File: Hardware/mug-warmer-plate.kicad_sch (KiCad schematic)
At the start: 32 parts, among them SW1 SW_DIP_x01, U1 LM35-NEB, U2 ATtiny85-20P

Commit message: Added test point to test thermoelectric cooler
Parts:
- added TP3, TP4: (no value), symbol Connector:TestPoint
- C9: value (none) -> 1uF; footprint (none) -> Capacitor_THT:C_Disc_D4.3mm_W1.9mm_P5.00mm
- J1: value (none) -> USB_C_Receptacle_USB2.0; footprint (none) -> USB_C_Power:TYPE-C-31-M-17
- J4: value (none) -> Conn_01x02_Male; footprint (none) -> Connector_PinHeader_2.54mm:PinHeader_1x04_P2.54mm_Vertical
- NT1: value (none) -> NetTie_2
- Q1: value (none) -> IRLZ44N; footprint (none) -> Package_TO_SOT_THT:TO-220-3_Vertical
- R1, R2, R3, R4, R5, R6, R7, R8: footprint (none) -> Resistor_THT:R_Axial_DIN0207_L6.3mm_D2.5mm_P10.16mm_Horizontal
- SW1: footprint (none) -> Button_Switch_THT:SW_PUSH_6mm_H4.3mm
- TP1, TP2: footprint (none) -> TestPoint:TestPoint_Pad_2.0x2.0mm
- U1: footprint (none) -> Package_TO_SOT_THT:TO-220-3_Horizontal_TabDown
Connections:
- net +5V: now also TP3.1
- net at C5.1, D2.1 (K), NT2.1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: now also TP4.1
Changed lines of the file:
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@@
     (company "KMBS Labs")
   )
+  (junction (at 139.7 162.56) (diameter 0) (color 0 0 0 0)
+  )
   (junction (at 121.92 140.97) (diameter 0) (color 0 0 0 0)
+  )
+  (junction (at 138.43 140.97) (diameter 0) (color 0 0 0 0)
   )
   (junction (at 242.57 101.6) (diameter 0) (color 0 0 0 0)
@@
     (in_bom yes) (on_board yes) (fields_autoplaced)
     (property "Reference" "NT1" (id 0) (at 140.97 135.89 0))
-    (property "Value" "" (id 1) (at 140.97 138.43 0))
+    (property "Value" "NetTie_2" (id 1) (at 140.97 138.43 0))
     (property "Footprint" "NetTie:NetTie-2_SMD_Pad0.5mm" (id 2) (at 140.97 140.97 0)
       (effects (font (size 1.27 1.27)) hide)
@@
     (pin "1")
   )
+  (symbol (lib_id "Connector:TestPoint") (at 139.7 162.56 0) (unit 1)
+    (in_bom yes) (on_board yes) (fields_autoplaced)
+    (property "Reference" "TP4" (id 0) (at 142.24 157.9879 0)
+      (effects (font (size 1.27 1.27)) (justify left))
+    )
+    (property "Value" "" (id 1) (at 142.24 160.5279 0)
+      (effects (font (size 1.27 1.27)) (justify left))
+    )
+    (property "Footprint" "" (id 2) (at 144.78 162.56 0)
+      (effects (font (size 1.27 1.27)) hide)
+    )
+    (property "Datasheet" "~" (id 3) (at 144.78 162.56 0)
+      (effects (font (size 1.27 1.27)) hide)
+    )
+    (pin "1")
+  )
   (symbol (lib_id "Device:R") (at 234.95 116.84 0) (unit 1)
     (in_bom yes) (on_board yes) (fields_autoplaced)
@@
       (effects (font (size 1.27 1.27)) (justify left))
     )
-    (property "Footprint" "" (id 2) (at 233.172 116.84 90)
+    (property "Footprint" "Resistor_THT:R_Axial_DIN0207_L6.3mm_D2.5mm_P10.16mm_Horizontal" (id 2) (at 233.172 116.84 90)
       (effects (font (size 1.27 1.27)) hide)
     )
@@
       (effects (font (size 1.27 1.27)) (justify right))
     )
-    (property "Value" "" (id 1) (at 255.27 104.1399 0)
-      (effects (font (size 1.27 1.27)) (justify right))
-    )
-    (property "Footprint" "" (id 2) (at 254 104.14 0)
+    (property "Value" "Conn_01x02_Male" (id 1) (at 255.27 104.1399 0)
+      (effects (font (size 1.27 1.27)) (justify right))
+    )
+    (property "Footprint" "Connector_PinHeader_2.54mm:PinHeader_1x04_P2.54mm_Vertical" (id 2) (at 254 104.14 0)
       (effects (font (size 1.27 1.27)) hide)
     )
@@
       (effects (font (size 1.27 1.27)) (justify left))
     )
-    (property "Footprint" "" (id 2) (at 121.412 179.07 90)
+    (property "Footprint" "Resistor_THT:R_Axial_DIN0207_L6.3mm_D2.5mm_P10.16mm_Horizontal" (id 2) (at 121.412 179.07 90)
       (effects (font (size 1.27 1.27)) hide)
     )
@@
       (effects (font (size 1.27 1.27)) (justify left))
     )
-    (property "Footprint" "" (id 2) (at 224.282 116.84 90)
+    (property "Footprint" "Resistor_THT:R_Axial_DIN0207_L6.3mm_D2.5mm_P10.16mm_Horizontal" (id 2) (at 224.282 116.84 90)
       (effects (font (size 1.27 1.27)) hide)
     )
@@
     (in_bom yes) (on_board yes) (fields_autoplaced)
     (property "Reference" "J1" (id 0) (at 38.1 27.94 0))
-    (property "Value" "" (id 1) (at 38.1 30.48 0))
-    (property "Footprint" "" (id 2) (at 41.91 50.8 0)
+    (property "Value" "USB_C_Receptacle_USB2.0" (id 1) (at 38.1 30.48 0))
+    (property "Footprint" "USB_C_Power:TYPE-C-31-M-17" (id 2) (at 41.91 50.8 0)
       (effects (font (size 1.27 1.27)) hide)
     )
@@
       (effects (font (size 1.27 1.27)) (justify right))
     )
-    (property "Value" "" (id 1) (at 111.76 180.34 0)
-      (effects (font (size 1.27 1.27)) (justify right))
-    )
-    (property "Footprint" "" (id 2) (at 117.1448 175.26 0)
+    (property "Value" "1uF" (id 1) (at 111.76 180.34 0)
+      (effects (font (size 1.27 1.27)) (justify right))
+    )
+    (property "Footprint" "Capacitor_THT:C_Disc_D4.3mm_W1.9mm_P5.00mm" (id 2) (at 117.1448 175.26 0)
       (effects (font (size 1.27 1.27)) hide)
     )
@@
       (effects (font (size 1.27 1.27)) (justify left))
     )
-    (property "Footprint" "" (id 2) (at 97.79 45.72 0)
+    (property "Footprint" "TestPoint:TestPoint_Pad_2.0x2.0mm" (id 2) (at 97.79 45.72 0)
       (effects (font (size 1.27 1.27)) hide)
     )
@@
       (effects (font (size 1.27 1.27)) (justify left))
     )
-    (property "Footprint" "" (id 2) (at 240.792 116.84 90)
+    (property "Footprint" "Resistor_THT:R_Axial_DIN0207_L6.3mm_D2.5mm_P10.16mm_Horizontal" (id 2) (at 240.792 116.84 90)
       (effects (font (size 1.27 1.27)) hide)
     )
@@
       (effects (font (size 1.27 1.27)) (justify right))
     )
-    (property "Footprint" "" (id 2) (at 266.7 71.12 0)
+    (property "Footprint" "Button_Switch_THT:SW_PUSH_6mm_H4.3mm" (id 2) (at 266.7 71.12 0)
       (effects (font (size 1.27 1.27)) hide)
     )
@@
       (effects (font (size 1.27 1.27)) (justify left))
     )
-    (property "Footprint" "" (id 2) (at 64.262 46.99 90)
+    (property "Footprint" "Resistor_THT:R_Axial_DIN0207_L6.3mm_D2.5mm_P10.16mm_Horizontal" (id 2) (at 64.262 46.99 90)
       (effects (font (size 1.27 1.27)) hide)
     )
@@
       (effects (font (size 1.27 1.27)) (justify left))
     )
-    (property "Footprint" "" (id 2) (at 73.152 46.99 90)
+    (property "Footprint" "Resistor_THT:R_Axial_DIN0207_L6.3mm_D2.5mm_P10.16mm_Horizontal" (id 2) (at 73.152 46.99 90)
       (effects (font (size 1.27 1.27)) hide)
     )
@@
       (effects (font (size 1.27 1.27)) (justify left))
     )
-    (property "Footprint" "" (id 2) (at 83.312 41.91 90)
+    (property "Footprint" "Resistor_THT:R_Axial_DIN0207_L6.3mm_D2.5mm_P10.16mm_Horizontal" (id 2) (at 83.312 41.91 90)
       (effects (font (size 1.27 1.27)) hide)
     )
@@
       (effects (font (size 1.27 1.27)) (justify left))
     )
-    (property "Value" "" (id 1) (at 138.43 171.4499 0)
-      (effects (font (size 1.27 1.27)) (justify left))
-    )
-    (property "Footprint" "" (id 2) (at 138.43 172.085 0)
+    (property "Value" "IRLZ44N" (id 1) (at 138.43 171.4499 0)
+      (effects (font (size 1.27 1.27)) (justify left))
+    )
+    (property "Footprint" "Package_TO_SOT_THT:TO-220-3_Vertical" (id 2) (at 138.43 172.085 0)
       (effects (font (size 1.27 1.27) italic) (justify left) hide)
     )
@@
       (effects (font (size 1.27 1.27)) (justify right))
     )
-    (property "Footprint" "" (id 2) (at 59.69 179.07 0)
+    (property "Footprint" "Package_TO_SOT_THT:TO-220-3_Horizontal_TabDown" (id 2) (at 59.69 179.07 0)
       (effects (font (size 1.27 1.27)) (justify left) hide)
     )
@@
   )
   (symbol (lib_id "Device:NetTie_2") (at 142.24 162.56 0) (unit 1)
-    (in_bom yes) (on_board yes) (fields_autoplaced)
-    (property "Reference" "NT2" (id 0) (at 142.24 157.48 0))
-    (property "Value" "NetTie_2" (id 1) (at 142.24 160.02 0))
+    (in_bom yes) (on_board yes)
+    (property "Reference" "NT2" (id 0) (at 142.24 165.1 0))
+    (property "Value" "NetTie_2" (id 1) (at 142.24 166.37 0))
     (property "Footprint" "NetTie:NetTie-2_SMD_Pad0.5mm" (id 2) (at 142.24 162.56 0)
       (effects (font (size 1.27 1.27)) hide)
@@
     (pin "2")
   )
+  (symbol (lib_id "Connector:TestPoint") (at 138.43 140.97 180) (unit 1)
+    (in_bom yes) (on_board yes) (fields_autoplaced)
+    (property "Reference" "TP3" (id 0) (at 140.97 143.0019 0)
+      (effects (font (size 1.27 1.27)) (justify right))
+    )
+    (property "Value" "" (id 1) (at 140.97 145.5419 0)
+      (effects (font (size 1.27 1.27)) (justify right))
+    )
+    (property "Footprint" "" (id 2) (at 133.35 140.97 0)
+      (effects (font (size 1.27 1.27)) hide)
+    )
+    (property "Datasheet" "~" (id 3) (at 133.35 140.97 0)
+      (effects (font (size 1.27 1.27)) hide)
+    )
+    (pin "1")
+  )
   (symbol (lib_id "Device:R") (at 266.7 85.09 0) (unit 1)
     (in_bom yes) (on_board yes) (fields_autoplaced)
@@
       (effects (font (size 1.27 1.27)) (justify left))
     )
-    (property "Footprint" "" (id 2) (at 264.922 85.09 90)
+    (property "Footprint" "Resistor_THT:R_Axial_DIN0207_L6.3mm_D2.5mm_P10.16mm_Horizontal" (id 2) (at 264.922 85.09 90)
       (effects (font (size 1.27 1.27)) hide)
     )
@@
       (effects (font (size 1.27 1.27)) (justify left))
     )
-    (property "Footprint" "" (id 2) (at 97.79 40.64 0)
+    (property "Footprint" "TestPoint:TestPoint_Pad_2.0x2.0mm" (id 2) (at 97.79 40.64 0)
       (effects (font (size 1.27 1.27)) hide)
     )
@@
       (reference "TP2") (unit 1) (value "TestPoint") (footprint "TestPoint:TestPoint_Pad_2.0x2.0mm")
     )
+    (path "/ddefb04a-3bc6-4293-84d9-1adacd82621e"
+      (reference "TP3") (unit 1) (value "TestPoint") (footprint "TestPoint:TestPoint_Pad_1.0x1.0mm")
+    )
+    (path "/2b984e20-8f25-40fa-af2c-f1f1931b43c0"
+      (reference "TP4") (unit 1) (value "TestPoint") (footprint "TestPoint:TestPoint_Pad_1.0x1.0mm")
+    )
     (path "/c3a44ace-7ce0-4e44-8650-439625bbdbd0"

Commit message: Completed silkscreen layer
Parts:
- TP1: value TestPoint -> (none); footprint TestPoint:TestPoint_Pad_2.0x2.0mm -> (none)
- TP2: value TestPoint -> (none)
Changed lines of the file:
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@@
       (effects (font (size 1.27 1.27)) (justify left))
     )
-    (property "Value" "TestPoint" (id 1) (at 102.87 41.9099 90)
+    (property "Value" "" (id 1) (at 102.87 41.9099 90)
       (effects (font (size 1.27 1.27)) (justify left))
     )
@@
       (effects (font (size 1.27 1.27)) (justify left))
     )
-    (property "Value" "TestPoint" (id 1) (at 102.87 36.8299 90)
-      (effects (font (size 1.27 1.27)) (justify left))
-    )
-    (property "Footprint" "TestPoint:TestPoint_Pad_2.0x2.0mm" (id 2) (at 97.79 40.64 0)
+    (property "Value" "" (id 1) (at 102.87 36.8299 90)
+      (effects (font (size 1.27 1.27)) (justify left))
+    )
+    (property "Footprint" "" (id 2) (at 97.79 40.64 0)
       (effects (font (size 1.27 1.27)) hide)
     )
@@
     )
     (path "/eab7c737-4450-406f-9f80-b2e18bb45dd6"
-      (reference "TP1") (unit 1) (value "TestPoint") (footprint "TestPoint:TestPoint_Pad_2.0x2.0mm")
+      (reference "TP1") (unit 1) (value "5V") (footprint "TestPoint:TestPoint_Pad_2.0x2.0mm")
     )
     (path "/829d375c-a6bc-4b11-a8ad-9aee4d2bbd98"
-      (reference "TP2") (unit 1) (value "TestPoint") (footprint "TestPoint:TestPoint_Pad_2.0x2.0mm")
+      (reference "TP2") (unit 1) (value "GND") (footprint "TestPoint:TestPoint_Pad_2.0x2.0mm")
     )
     (path "/ddefb04a-3bc6-4293-84d9-1adacd82621e"
-      (reference "TP3") (unit 1) (value "TestPoint") (footprint "TestPoint:TestPoint_Pad_1.0x1.0mm")
+      (reference "TP3") (unit 1) (value "5V") (footprint "TestPoint:TestPoint_Pad_2.0x2.0mm")
     )
     (path "/2b984e20-8f25-40fa-af2c-f1f1931b43c0"
-      (reference "TP4") (unit 1) (value "TestPoint") (footprint "TestPoint:TestPoint_Pad_1.0x1.0mm")
+      (reference "TP4") (unit 1) (value "GND") (footprint "TestPoint:TestPoint_Pad_2.0x2.0mm")
     )
     (path "/c3a44ace-7ce0-4e44-8650-439625bbdbd0"

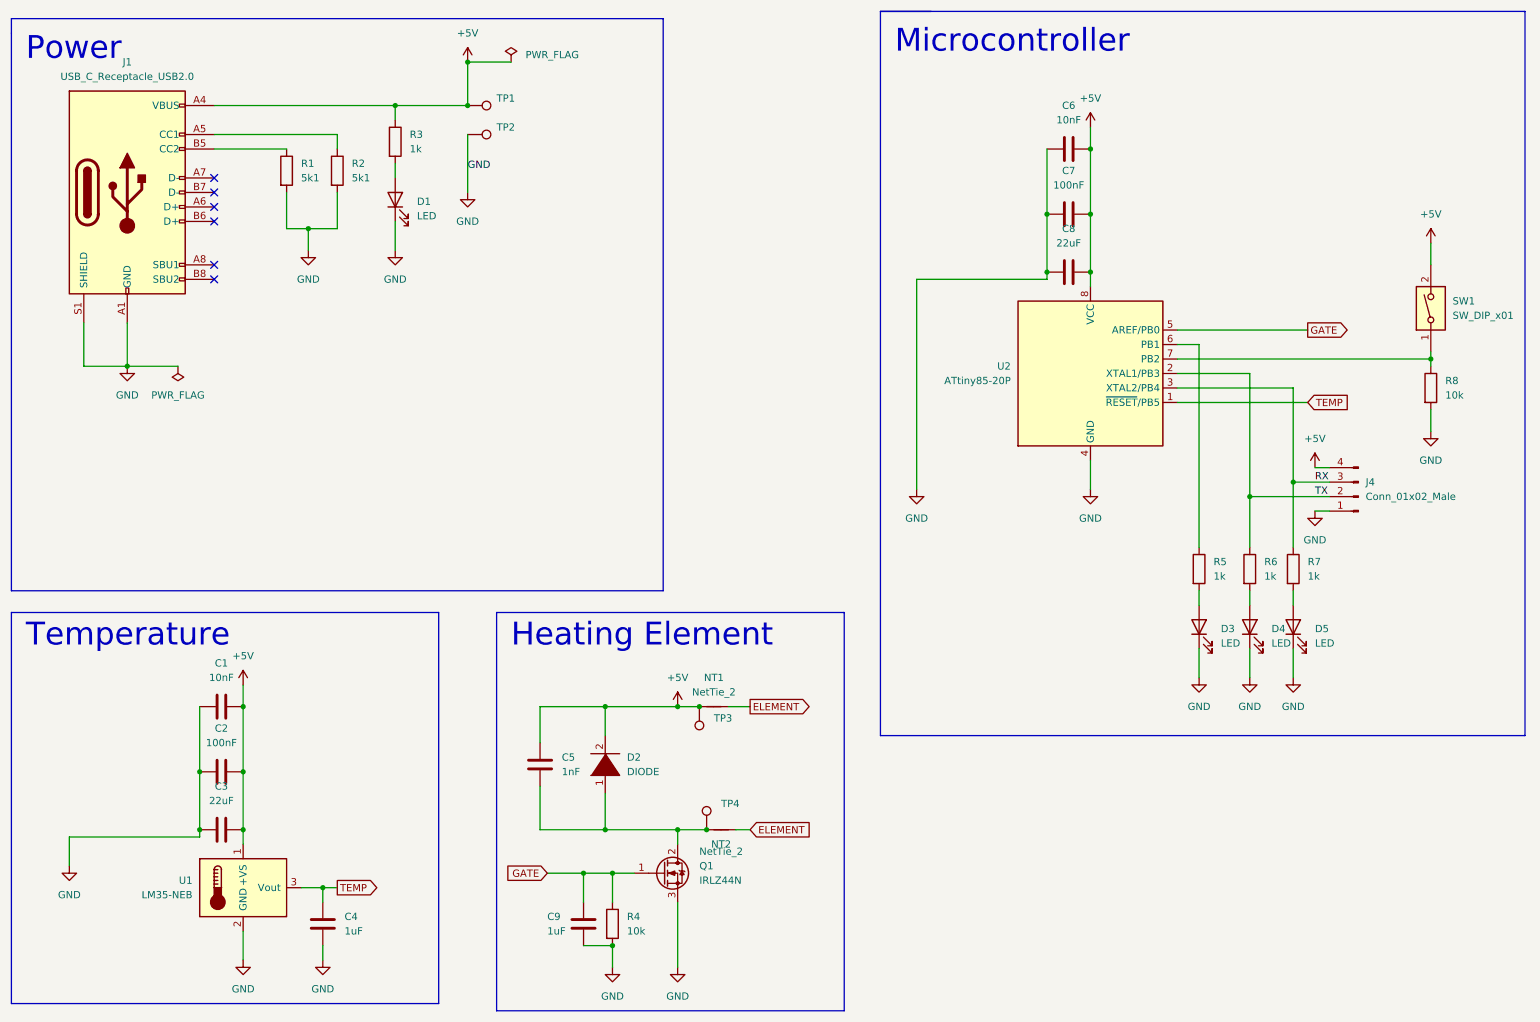
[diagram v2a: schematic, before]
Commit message: Add 2V bias to TEMP pin to prevent ATTiny85 from resetting
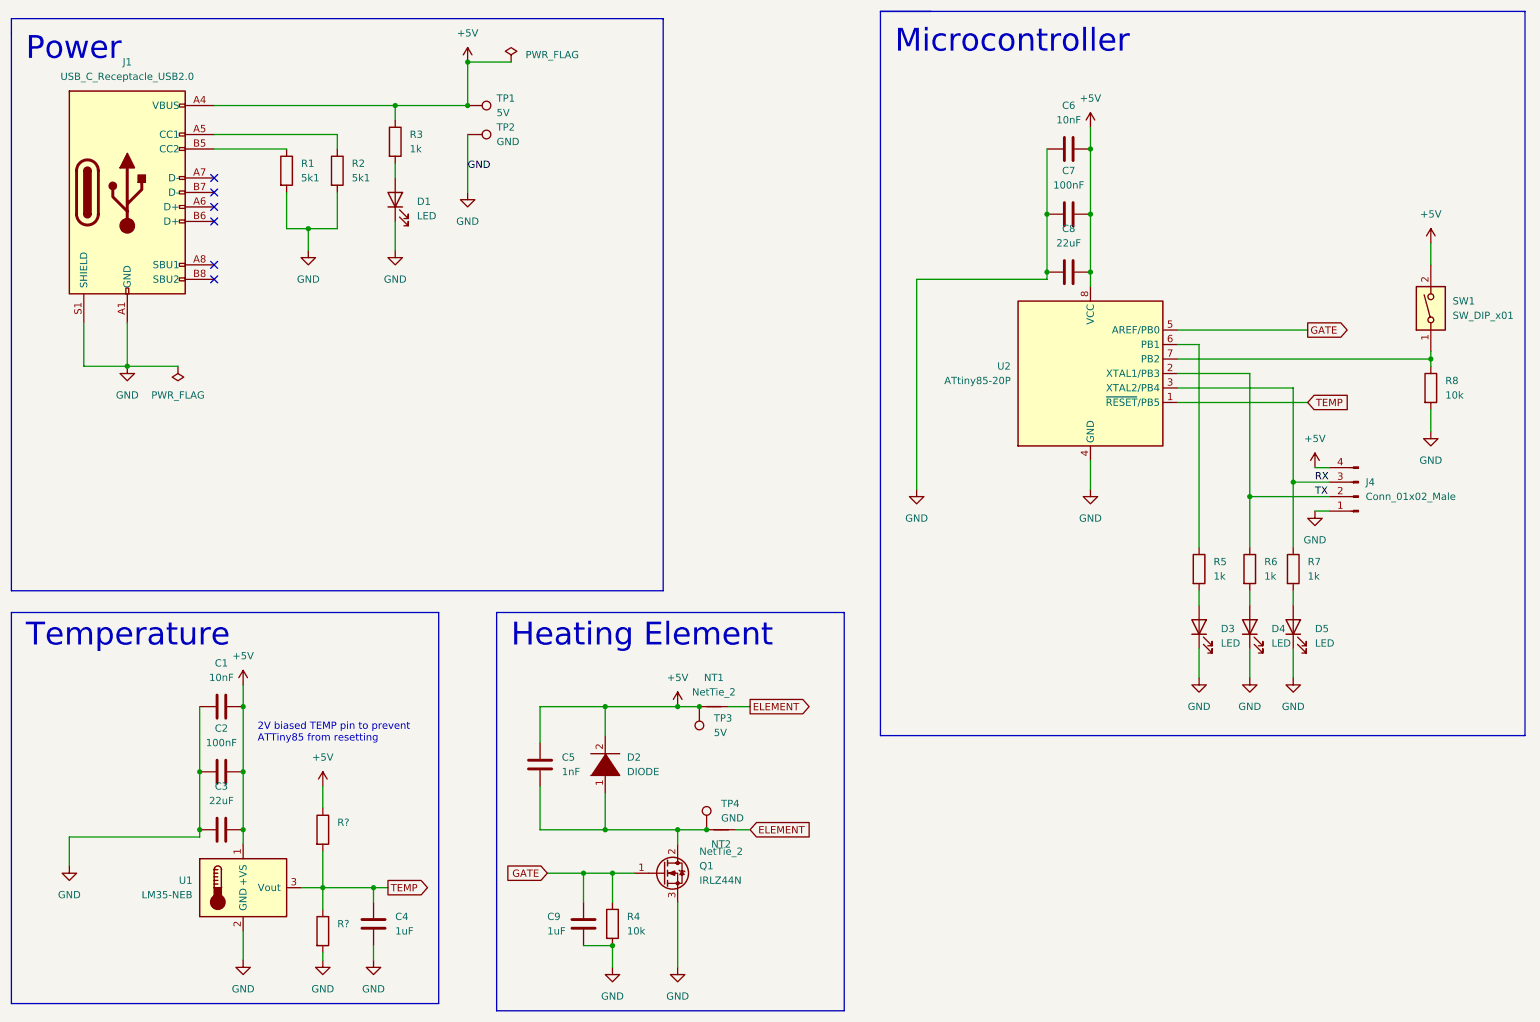
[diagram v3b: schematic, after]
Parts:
- added R? (x2): (no value), Resistor_THT:R_Axial_DIN0207_L6.3mm_D2.5mm_P10.16mm_Horizontal, symbol Device:R
- TP1, TP3: value (none) -> 5V; footprint (none) -> TestPoint:TestPoint_Pad_2.0x2.0mm
- TP2: value (none) -> GND
- TP4: value (none) -> GND; footprint (none) -> TestPoint:TestPoint_Pad_2.0x2.0mm
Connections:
- net +5V: now also R?.1
- net GND: now also R?.2
- net TEMP: now also R?.1, R?.2
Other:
- note added: "2V biased TEMP pin to prevent ATTiny85 from resetting"
- moved on the sheet: C4
